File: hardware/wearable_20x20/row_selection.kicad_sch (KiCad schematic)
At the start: 75 parts, among them Q201 AO3403, Q202 AO3403, Q203 AO3403, Q204 AO3403, Q205 AO3403, Q206 AO3403, Q207 AO3403, Q208 AO3403, Q209 AO3403, Q210 AO3403, Q211 AO3403, Q212 AO3403, Q213 AO3403, Q214 AO3403, Q215 AO3403, Q216 AO3403, Q217 AO3403, Q218 AO3403, Q219 AO3403, Q220 AO3403, U201 SN74LVC8T245RHLR, U202 74HC154PW,118, U203 74HC154PW,118

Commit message: Clarify unused translator input grounding
Co-authored-by: illiapliukhin <illiapliukhin@users.noreply.github.com>
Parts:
- added R408, R409: 0R, Resistor_SMD:R_0603_1608Metric, symbol Device:R
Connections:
- net GND: now also R408.1, R409.1; no longer U201.10 (A8), U201.9 (A7)
- new net ROW_XLAT_A7_UNUSED: R408.2, U201.9 (A7)
- new net ROW_XLAT_A8_UNUSED: R409.2, U201.10 (A8)
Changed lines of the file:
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@@
 		)
 	)
+	(label "ROW_XLAT_A7_UNUSED"
+		(at 87.63 93.98 0)
+		(effects
+			(font
+				(size 1.27 1.27)
+			)
+			(justify left bottom)
+		)
+	)
 	(label "ROW_A2_4V1"
 		(at 87.63 58.42 0)
@@
 		)
 	)
-	(label "GND"
-		(at 45.72 68.58 0)
-		(effects
-			(font
-				(size 1.27 1.27)
-			)
-			(justify left bottom)
-		)
-	)
 	(label "U202_Y06_N"
 		(at 102.87 198.12 0)
@@
 		)
 	)
+	(label "ROW_XLAT_A8_UNUSED"
+		(at 87.63 101.6 0)
+		(effects
+			(font
+				(size 1.27 1.27)
+			)
+			(justify left bottom)
+		)
+	)
 	(label "ROW_20_GATE"
 		(at 196.85 185.42 180)
@@
 		)
 	)
+	(label "GND"
+		(at 80.01 101.6 180)
+		(effects
+			(font
+				(size 1.27 1.27)
+			)
+			(justify right bottom)
+		)
+	)
 	(label "DEC_B_EN_N"
 		(at 45.72 63.5 0)
@@
 		)
 	)
+	(label "GND"
+		(at 80.01 93.98 180)
+		(effects
+			(font
+				(size 1.27 1.27)
+			)
+			(justify right bottom)
+		)
+	)
 	(label "U202_Y15_N"
 		(at 139.7 76.2 180)
@@
 		)
 	)
+	(label "ROW_XLAT_A8_UNUSED"
+		(at 45.72 73.66 0)
+		(effects
+			(font
+				(size 1.27 1.27)
+			)
+			(justify left bottom)
+		)
+	)
 	(label "ROW_20_GATE"
 		(at 213.36 185.42 0)
@@
 		)
 	)
+	(label "ROW_XLAT_A7_UNUSED"
+		(at 45.72 68.58 0)
+		(effects
+			(font
+				(size 1.27 1.27)
+			)
+			(justify left bottom)
+		)
+	)
 	(label "LED_4V1"
 		(at 214.63 114.3 180)
@@
 		)
 	)
-	(label "GND"
-		(at 45.72 73.66 0)
-		(effects
-			(font
-				(size 1.27 1.27)
-			)
-			(justify left bottom)
-		)
-	)
 	(label "ROW_14_ANODE"
 		(at 119.38 281.94 90)
@@
 	)
 	(symbol
+		(lib_id "Device:R")
+		(at 83.82 101.6 90)
+		(unit 1)
+		(body_style 1)
+		(exclude_from_sim no)
+		(in_bom yes)
+		(on_board yes)
+		(in_pos_files yes)
+		(dnp no)
+		(property "Reference" "R409"
+			(at 83.82 103.632 180)
+			(show_name no)
+			(do_not_autoplace no)
+			(effects
+				(font
+					(size 1.27 1.27)
+				)
+				(justify left)
+			)
+		)
+		(property "Value" "0R"
+			(at 83.82 101.6 180)
+			(show_name no)
+			(do_not_autoplace no)
+			(effects
+				(font
+					(size 1.27 1.27)
+				)
+				(justify left)
+			)
+		)
+		(property "Footprint" "Resistor_SMD:R_0603_1608Metric"
+			(at 82.042 101.6 90)
+			(hide yes)
+			(show_name no)
+			(do_not_autoplace no)
+			(effects
+				(font
+					(size 1.27 1.27)
+				)
+			)
+		)
+		(property "Datasheet" ""
+			(at 83.82 101.6 0)
+			(show_name no)
+			(do_not_autoplace no)
+			(effects
+				(font
+					(size 1.27 1.27)
+				)
+			)
+		)
+		(property "Description" ""
+			(at 83.82 101.6 0)
+			(show_name no)
+			(do_not_autoplace no)
+			(effects
+				(font
+					(size 1.27 1.27)
+				)
+			)
+		)
+		(property "Function" "ROW_XLAT_A8_GROUND_LINK"
+			(at 86.36 106.6799 0)
+			(show_name no)
+			(do_not_autoplace no)
+			(effects
+				(font
+					(size 1.27 1.27)
+				)
+				(justify left)
+			)
+		)
+		(pin "1"
+		)
+		(pin "2"
+		)
+		(instances
+			(project "row_selection"
+				(path "/1ea4952c-cf84-5739-b8b2-3d6a71ef719a"
+					(reference "R409")
+					(unit 1)
+				)
+			)
+		)
+	)
+	(symbol
 		(lib_id "Transistor_FET:Q_PMOS_GSD")
 		(at 116.84 287.02 0)
@@
 					(unit 1)
 				)
+			)
+		)
+	)
+	(symbol
+		(lib_id "Device:R")
+		(at 83.82 93.98 90)
+		(unit 1)
+		(body_style 1)
+		(exclude_from_sim no)
+		(in_bom yes)
+		(on_board yes)
+		(in_pos_files yes)
+		(dnp no)
+		(property "Reference" "R408"
+			(at 83.82 96.012 180)
+			(show_name no)
+			(do_not_autoplace no)
+			(effects
+				(font
+					(size 1.27 1.27)
+				)
+				(justify left)
+			)
+		)
+		(property "Value" "0R"
+			(at 83.82 93.98 180)
+			(show_name no)
+			(do_not_autoplace no)
+			(effects
+				(font
+					(size 1.27 1.27)
+				)
+				(justify left)
+			)
+		)
+		(property "Footprint" "Resistor_SMD:R_0603_1608Metric"
+			(at 82.042 93.98 90)
+			(hide yes)
+			(show_name no)
+			(do_not_autoplace no)
+			(effects
+				(font
+					(size 1.27 1.27)
+				)
+			)
+		)
+		(property "Datasheet" ""
+			(at 83.82 93.98 0)
+			(show_name no)
+			(do_not_autoplace no)
+			(effects
+				(font
+					(size 1.27 1.27)
+				)
+			)
+		)
+		(property "Description" ""
+			(at 83.82 93.98 0)
+			(show_name no)
+			(do_not_autoplace no)
+			(effects
+				(font
+					(size 1.27 1.27)
+				)
+			)
+		)
+		(property "Function" "ROW_XLAT_A7_GROUND_LINK"
+			(at 86.36 99.0599 0)
+			(show_name no)
+			(do_not_autoplace no)
+			(effects
+				(font
+					(size 1.27 1.27)
+				)
+				(justify left)
+			)
+		)
+		(pin "1"
+		)
+		(pin "2"
+		)
+		(instances
+			(project "row_selection"
+				(path "/1ea4952c-cf84-5739-b8b2-3d6a71ef719a"
+					(reference "R408")
+					(unit 1)
+				)

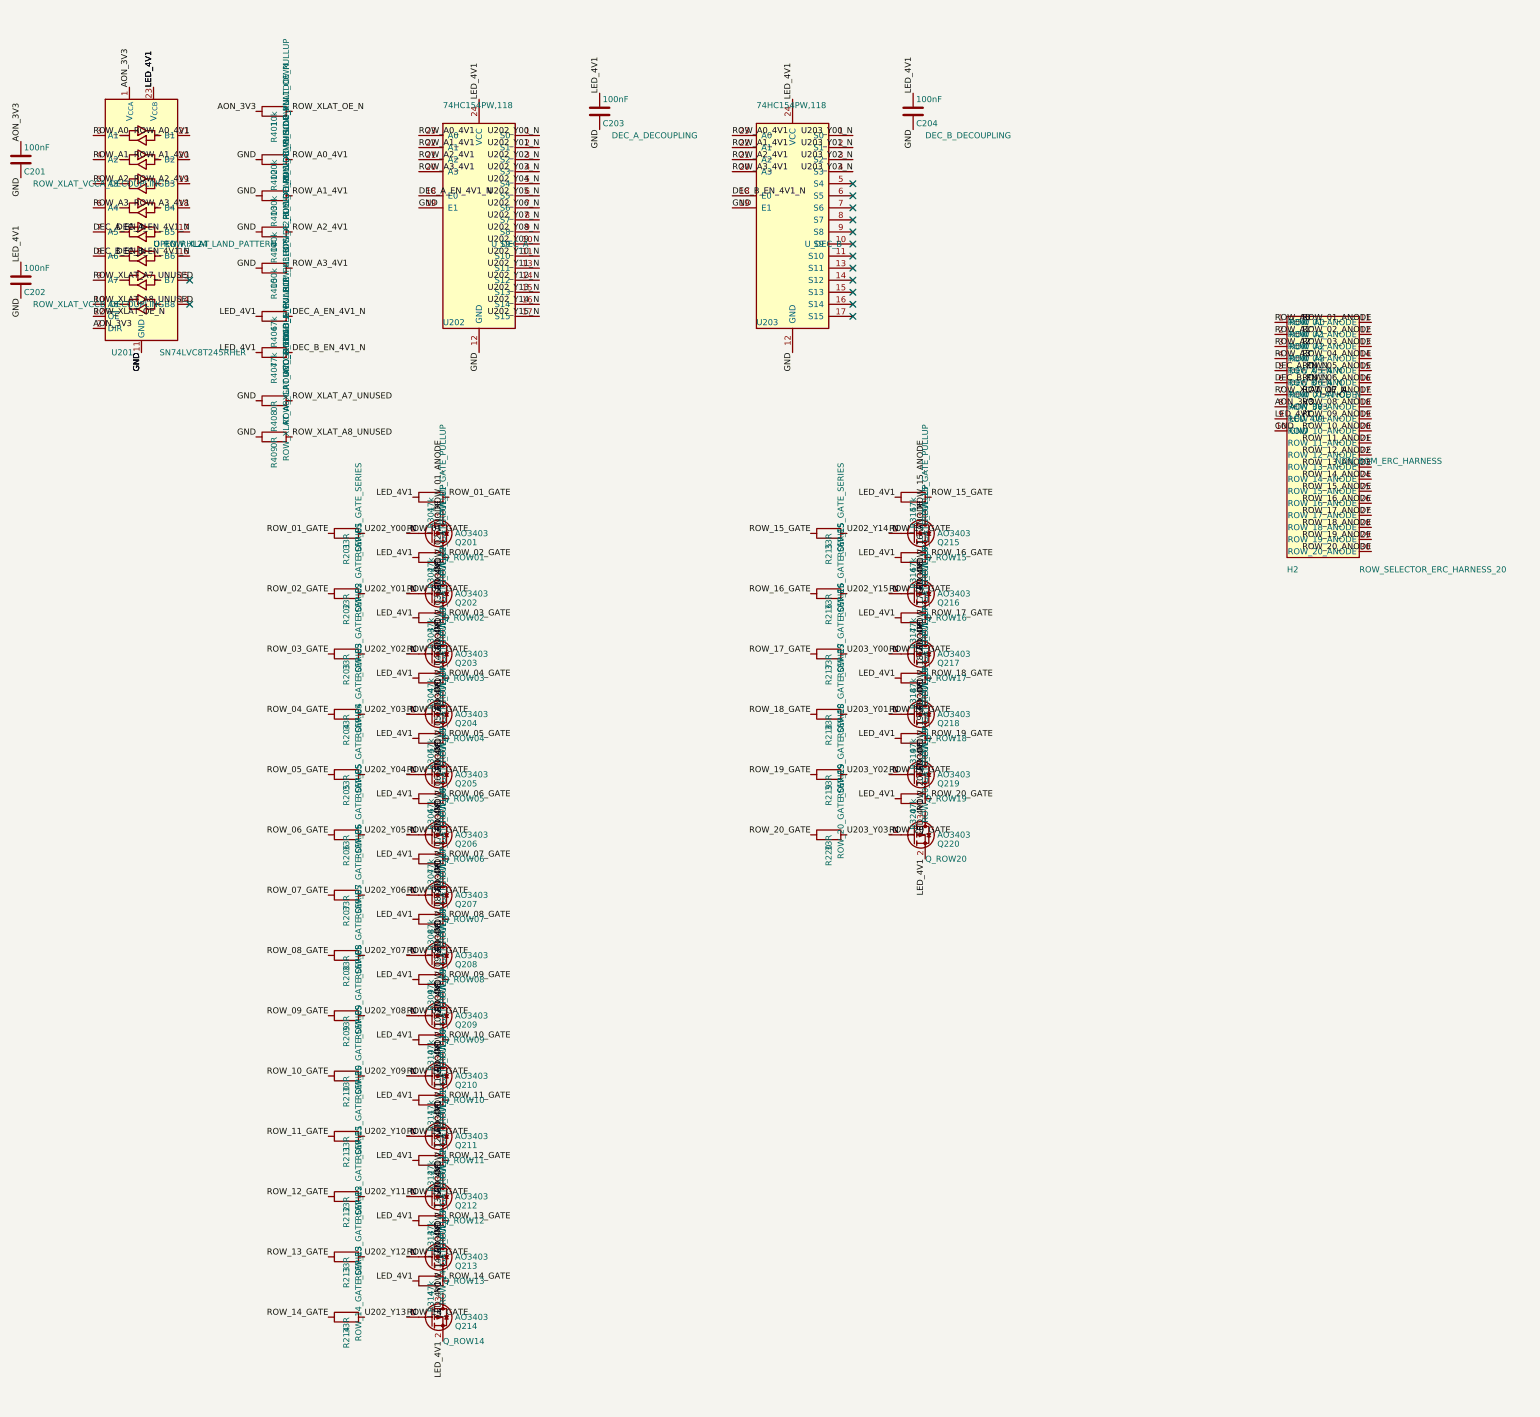
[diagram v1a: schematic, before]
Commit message: Preserve row resistor pin mapping
Co-authored-by: illiapliukhin <illiapliukhin@users.noreply.github.com>
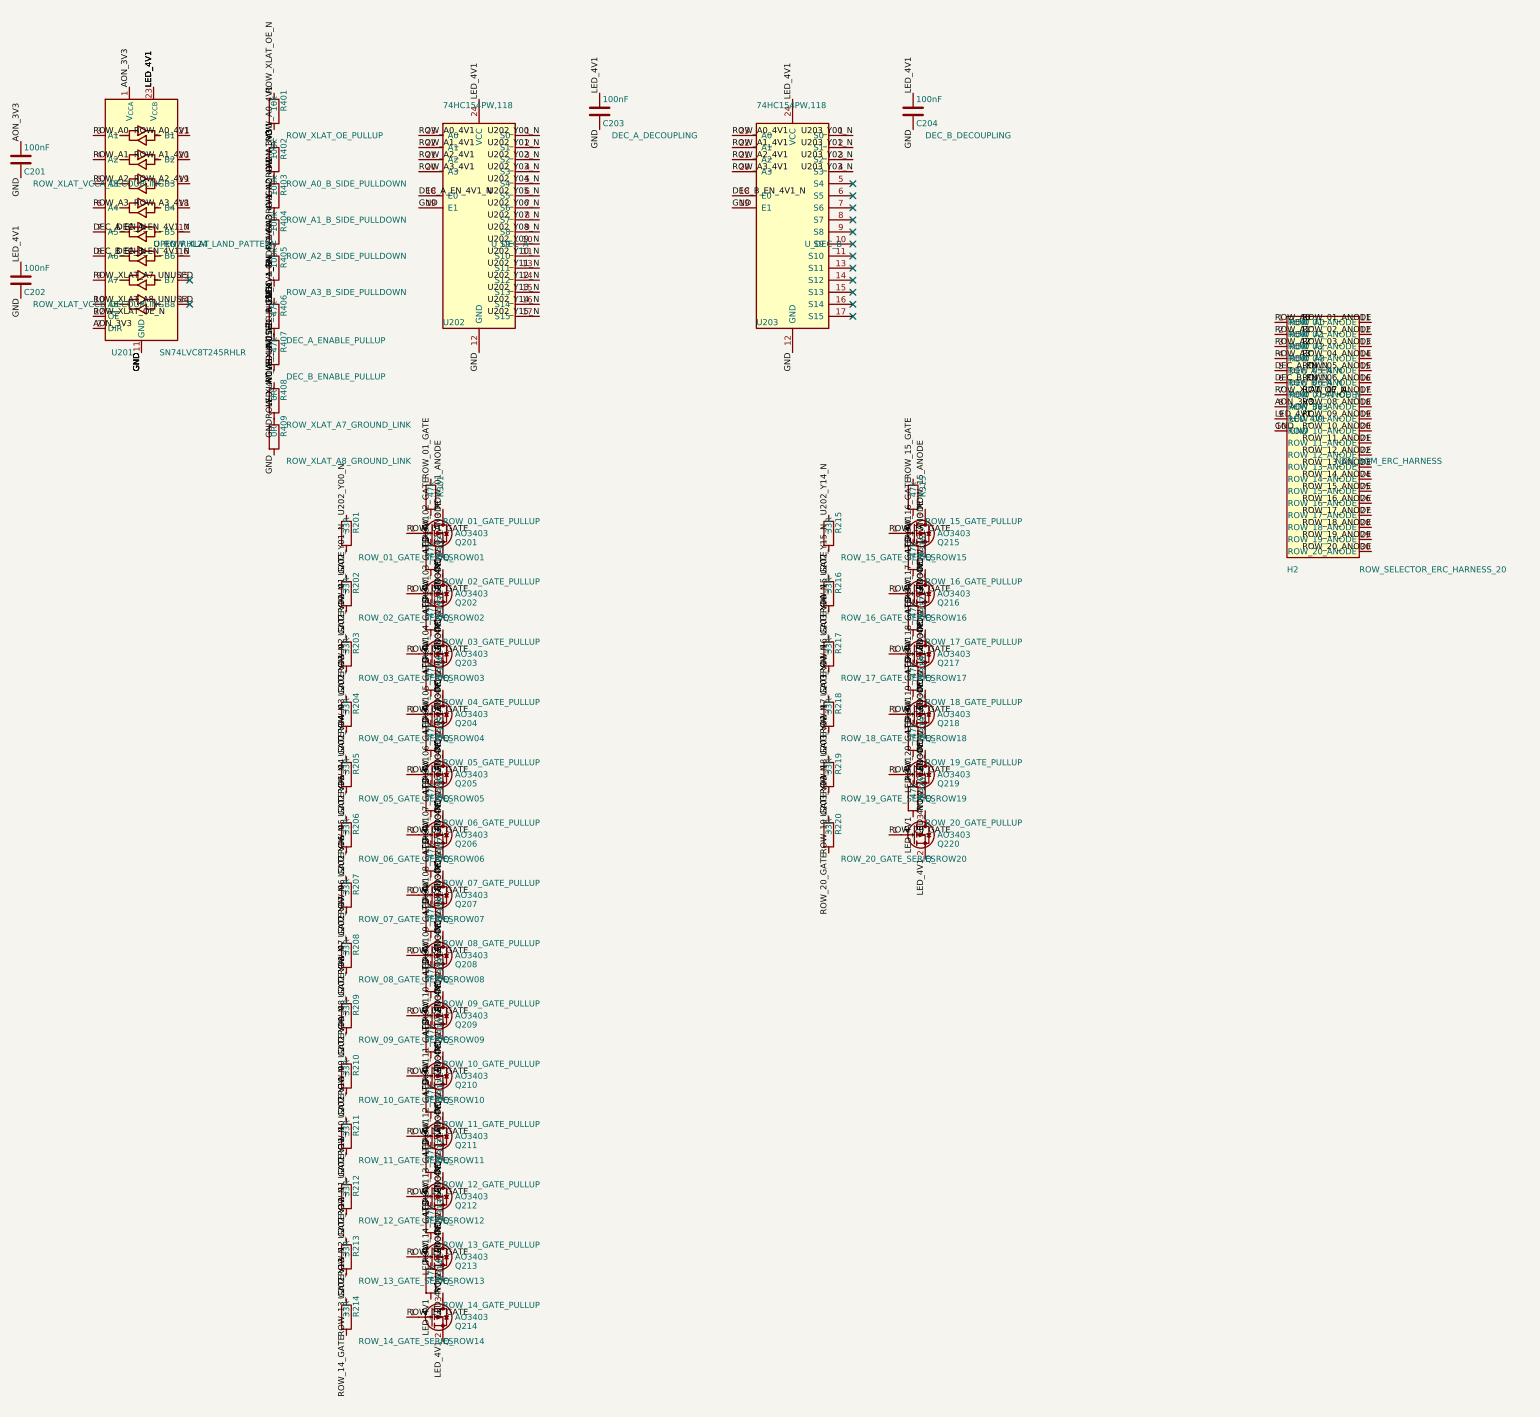
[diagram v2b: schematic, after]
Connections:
- net ROW_A1_4V1 is gone; now on net GND: R403.2, U201.20 (B2), U202.22 (A1), U203.22 (A1)
- net ROW_A2_4V1 is gone; now on net GND: R404.2, U201.19 (B3), U202.21 (A2), U203.21 (A2)
- net ROW_A3_4V1 is gone; now on net GND: R405.2, U201.18 (B4), U202.20 (A3), U203.20 (A3)
- net ROW_XLAT_A8_UNUSED is gone; now on net GND: R409.2, U201.10 (A8)
- net AON_3V3: now also R401.2; no longer R401.1
- net DEC_A_EN_4V1_N: now also R406.1; no longer R406.2
- net DEC_B_EN_4V1_N: now also C202.1, C203.1, C204.1, H2.9 (LED_4V1), Q201.2 (S), Q202.2 (S), Q203.2 (S), Q204.2 (S), Q205.2 (S), Q206.2 (S), Q207.2 (S), Q208.2 (S), Q209.2 (S), Q210.2 (S), Q211.2 (S), Q212.2 (S), Q213.2 (S), Q214.2 (S), Q215.2 (S), Q216.2 (S), Q217.2 (S), Q218.2 (S), Q219.2 (S), Q220.2 (S), R301.2, R302.2, R303.2, R304.2, R305.2, R306.2, R307.2, R308.2, R309.2, R310.2, R311.2, R312.2, R313.2, R314.2, R315.2, R316.2, R317.2, R318.2, R319.2, R320.2, R406.2, R407.1, U201.23 (V_{CCB}), U201.24 (V_{CCB}), U202.24 (VCC), U203.24 (VCC)
- net GND: now also R402.2, R408.2; no longer R402.1, R408.1
- net ROW_01_GATE: now also R201.2, R301.1; no longer R201.1, R301.2
- net ROW_02_GATE: now also R202.2, R302.1; no longer R202.1, R302.2
- net ROW_03_GATE: now also R203.2, R303.1; no longer R203.1, R303.2
- net ROW_04_GATE: now also R204.2, R304.1; no longer R204.1, R304.2
- net ROW_05_GATE: now also R205.2, R305.1; no longer R205.1, R305.2
- net ROW_06_GATE: now also R206.2, R306.1; no longer R206.1, R306.2
- net ROW_07_GATE: now also R207.2, R307.1; no longer R207.1, R307.2
- net ROW_08_GATE: now also R208.2, R308.1; no longer R208.1, R308.2
- net ROW_09_GATE: now also R209.2, R309.1; no longer R209.1, R309.2
- net ROW_10_GATE: now also R210.2, R310.1; no longer R210.1, R310.2
- net ROW_11_GATE: now also R211.2, R311.1; no longer R211.1, R311.2
- net ROW_12_GATE: now also R212.2, R312.1; no longer R212.1, R312.2
- net ROW_13_GATE: now also R213.2, R313.1; no longer R213.1, R313.2
- net ROW_14_GATE: now also R214.2, R314.1; no longer R214.1, R314.2
- net ROW_15_GATE: now also R215.2, R315.1; no longer R215.1, R315.2
- net ROW_16_GATE: now also R216.2, R316.1; no longer R216.1, R316.2
- net ROW_17_GATE: now also R217.2, R317.1; no longer R217.1, R317.2
- net ROW_18_GATE: now also R218.2, R318.1; no longer R218.1, R318.2
- net ROW_19_GATE: now also R219.2, R319.1; no longer R219.1, R319.2
- net ROW_20_GATE: now also R220.2, R320.1; no longer R220.1, R320.2
- net ROW_A0_4V1: now also R402.1; no longer R402.2
- net ROW_XLAT_A7_UNUSED: now also R408.1; no longer R408.2
- net ROW_XLAT_OE_N: now also R401.1; no longer R401.2
- net U202_Y00_N: now also R201.1; no longer R201.2
- net U202_Y01_N: now also R202.1; no longer R202.2
- net U202_Y02_N: now also R203.1; no longer R203.2
- net U202_Y03_N: now also R204.1; no longer R204.2
- net U202_Y04_N: now also R205.1; no longer R205.2
- net U202_Y05_N: now also R206.1; no longer R206.2
- net U202_Y06_N: now also R207.1; no longer R207.2
- net U202_Y07_N: now also R208.1; no longer R208.2
- net U202_Y08_N: now also R209.1; no longer R209.2
- net U202_Y09_N: now also R210.1; no longer R210.2
- net U202_Y10_N: now also R211.1; no longer R211.2
- net U202_Y11_N: now also R212.1; no longer R212.2
- net U202_Y12_N: now also R213.1; no longer R213.2
- net U202_Y13_N: now also R214.1; no longer R214.2
- net U202_Y14_N: now also R215.1; no longer R215.2
- net U202_Y15_N: now also R216.1; no longer R216.2
- net U203_Y00_N: now also R217.1; no longer R217.2
- net U203_Y01_N: now also R218.1; no longer R218.2
- net U203_Y02_N: now also R219.1; no longer R219.2
- net U203_Y03_N: now also R220.1; no longer R220.2
- removed net LED_4V1: C202.1, C203.1, C204.1, H2.9 (LED_4V1), Q201.2 (S), Q202.2 (S), Q203.2 (S), Q204.2 (S), Q205.2 (S), Q206.2 (S), Q207.2 (S), Q208.2 (S), Q209.2 (S), Q210.2 (S), Q211.2 (S), Q212.2 (S), Q213.2 (S), Q214.2 (S), Q215.2 (S), Q216.2 (S), Q217.2 (S), Q218.2 (S), Q219.2 (S), Q220.2 (S), R301.1, R302.1, R303.1, R304.1, R305.1, R306.1, R307.1, R308.1, R309.1, R310.1, R311.1, R312.1, R313.1, R314.1, R315.1, R316.1, R317.1, R318.1, R319.1, R320.1, R406.1, R407.1, U201.23 (V_{CCB}), U201.24 (V_{CCB}), U202.24 (VCC), U203.24 (VCC)
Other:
- moved on the sheet: R201, R202, R203, R204, R205, R206, R207, R208, R209, R210, R211, R212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

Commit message: Separate row resistor label endpoints
Co-authored-by: illiapliukhin <illiapliukhin@users.noreply.github.com>
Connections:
- net DEC_B_EN_4V1_N: no longer C202.1, C203.1, C204.1, H2.9 (LED_4V1), Q201.2 (S), Q202.2 (S), Q203.2 (S), Q204.2 (S), Q205.2 (S), Q206.2 (S), Q207.2 (S), Q208.2 (S), Q209.2 (S), Q210.2 (S), Q211.2 (S), Q212.2 (S), Q213.2 (S), Q214.2 (S), Q215.2 (S), Q216.2 (S), Q217.2 (S), Q218.2 (S), Q219.2 (S), Q220.2 (S), R301.2, R302.2, R303.2, R304.2, R305.2, R306.2, R307.2, R308.2, R309.2, R310.2, R311.2, R312.2, R313.2, R314.2, R315.2, R316.2, R317.2, R318.2, R319.2, R320.2, R406.2, R407.2, U201.23 (V_{CCB}), U201.24 (V_{CCB}), U202.24 (VCC), U203.24 (VCC)
- net GND: no longer R403.1, R404.1, R405.1, R409.1, U201.10 (A8), U201.18 (B4), U201.19 (B3), U201.20 (B2), U202.20 (A3), U202.21 (A2), U202.22 (A1), U203.20 (A3), U203.21 (A2), U203.22 (A1)
- new net LED_4V1: C202.1, C203.1, C204.1, H2.9 (LED_4V1), Q201.2 (S), Q202.2 (S), Q203.2 (S), Q204.2 (S), Q205.2 (S), Q206.2 (S), Q207.2 (S), Q208.2 (S), Q209.2 (S), Q210.2 (S), Q211.2 (S), Q212.2 (S), Q213.2 (S), Q214.2 (S), Q215.2 (S), Q216.2 (S), Q217.2 (S), Q218.2 (S), Q219.2 (S), Q220.2 (S), R301.2, R302.2, R303.2, R304.2, R305.2, R306.2, R307.2, R308.2, R309.2, R310.2, R311.2, R312.2, R313.2, R314.2, R315.2, R316.2, R317.2, R318.2, R319.2, R320.2, R406.2, R407.2, U201.23 (V_{CCB}), U201.24 (V_{CCB}), U202.24 (VCC), U203.24 (VCC)
- new net ROW_A1_4V1: R403.1, U201.20 (B2), U202.22 (A1), U203.22 (A1)
- new net ROW_A2_4V1: R404.1, U201.19 (B3), U202.21 (A2), U203.21 (A2)
- new net ROW_A3_4V1: R405.1, U201.18 (B4), U202.20 (A3), U203.20 (A3)
- new net ROW_XLAT_A8_UNUSED: R409.1, U201.10 (A8)
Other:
- moved on the sheet: R201, R202, R203, R204, R205, R206, R207, R208, R209, R210, R211, R212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

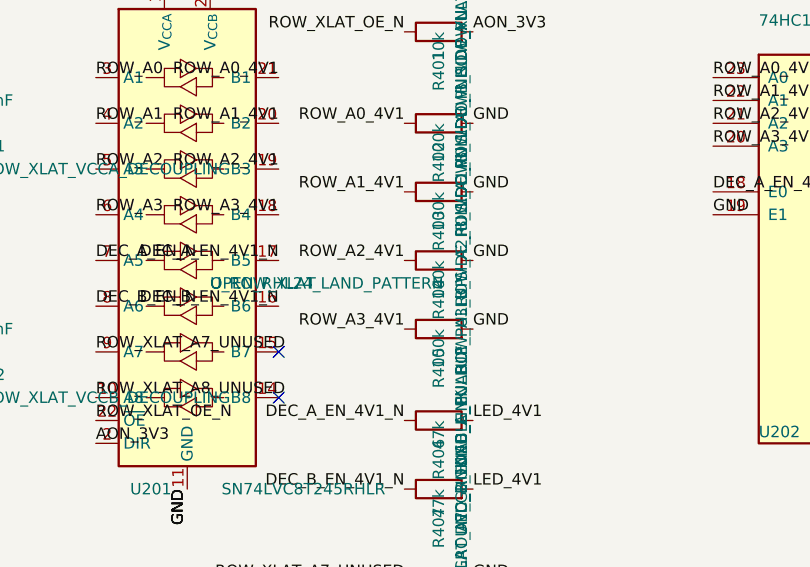
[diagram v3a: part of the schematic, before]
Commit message: Freeze mechanical inputs and RHL footprint
Co-authored-by: illiapliukhin <illiapliukhin@users.noreply.github.com>
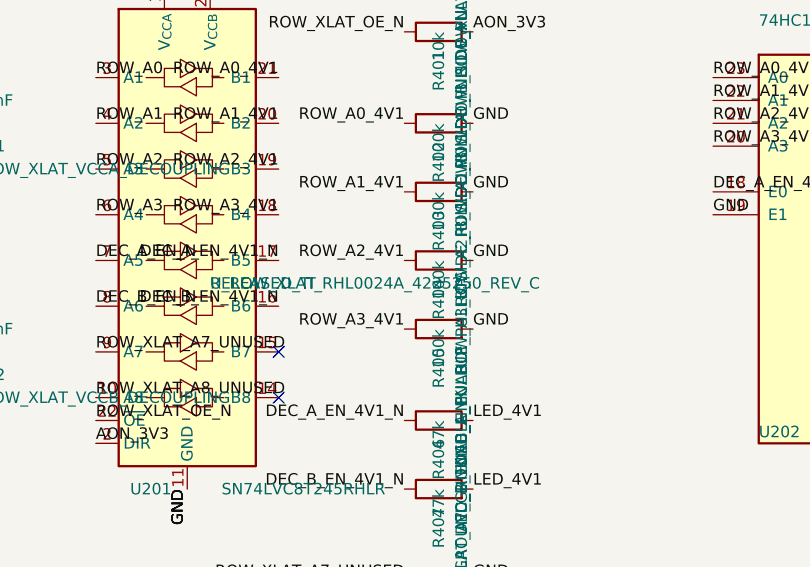
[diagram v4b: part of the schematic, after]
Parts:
- U201: footprint (none) -> PartSignal_Packages:TI_RHL0024A_VQFN-24-1EP_3.5x5.5mm_P0.5mm_EP2.05x4.05mm; FootprintStatus OPEN_RHL24_LAND_PATTERN -> RELEASED_TI_RHL0024A_4225250_REV_C
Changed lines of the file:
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@@
 			)
 		)
-		(property "Footprint" ""
+		(property "Footprint" "PartSignal_Packages:TI_RHL0024A_VQFN-24-1EP_3.5x5.5mm_P0.5mm_EP2.05x4.05mm"
 			(at 76.2 31.75 0)
 			(hide yes)
@@
 			)
 		)
-		(property "FootprintStatus" "OPEN_RHL24_LAND_PATTERN"
+		(property "FootprintStatus" "RELEASED_TI_RHL0024A_4225250_REV_C"
 			(at 58.42 60.9599 0)
 			(show_name no)
